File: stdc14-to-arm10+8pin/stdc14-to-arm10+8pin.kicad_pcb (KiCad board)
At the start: 2 copper layers, 26 x 41 mm, 3 parts, among them J1 Conn_ARM_JTAG_SWD_10, J2 Conn_ST_STDC14, J3 Conn_02x04_Counter_Clockwise

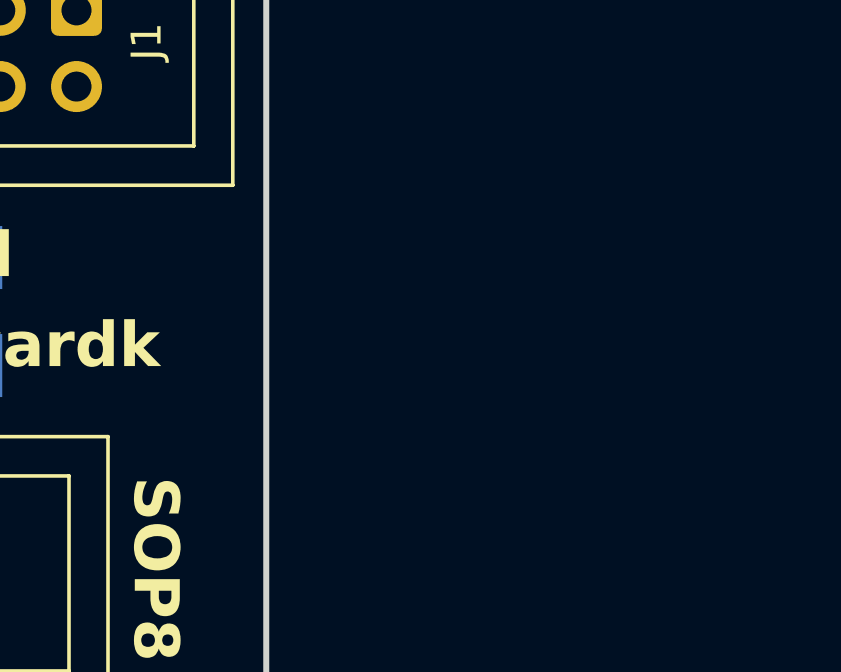
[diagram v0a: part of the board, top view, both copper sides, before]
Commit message: put soicbite onto pcb
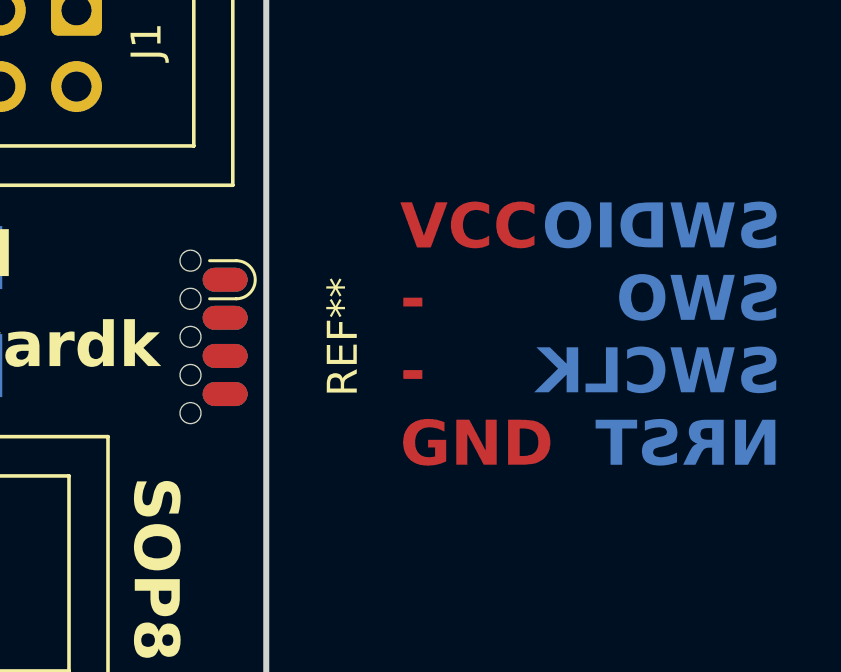
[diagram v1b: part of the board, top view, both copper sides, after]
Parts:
- added REF**: CONN_soicProgSmall, swd-converter:SOIC_clipProgSmall, F.Cu at (126.4, 93.3)
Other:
- board text added: "SWDIO SWO SWCLK NRST"
- board text added: "VCC - - GND"
